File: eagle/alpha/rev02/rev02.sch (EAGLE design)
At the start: 404 parts, among them CN1 HOST, CN2 HOST, IC1 N25Q128A13ES, IC2 74AC244DW, IC3 N25Q128A13ES, IC4 74AC244DW, IC5 RCLAMP0502ASC-89, IC6 RCLAMP0502ASC-89, J1 STM32-SWD, Q1 2N7002, Q2 BC818, Q4 2N7002, Q5 ASFL1, Q6 2N7002, T1 BC847, T2 BC847, U1 LMZ13608, U10 ATTINY828R-AU, U12 23K640-I/SN, U13 XC7A200TFBG484, U14 EN6347QI, U15 EN6347QI, U16 EN5364QI, U2 LT3060ITS8-15, U3 MC74HC1G14DTT1G, U4 STM32F429BIT6, U5 IS45S32160F, U6 IS45S32160F, U7 MCP79412-I/SN, U8 FT232H_SERIAL, U9 FT232H_SERIAL, Y1 12 MHz, Y2 12 MHz

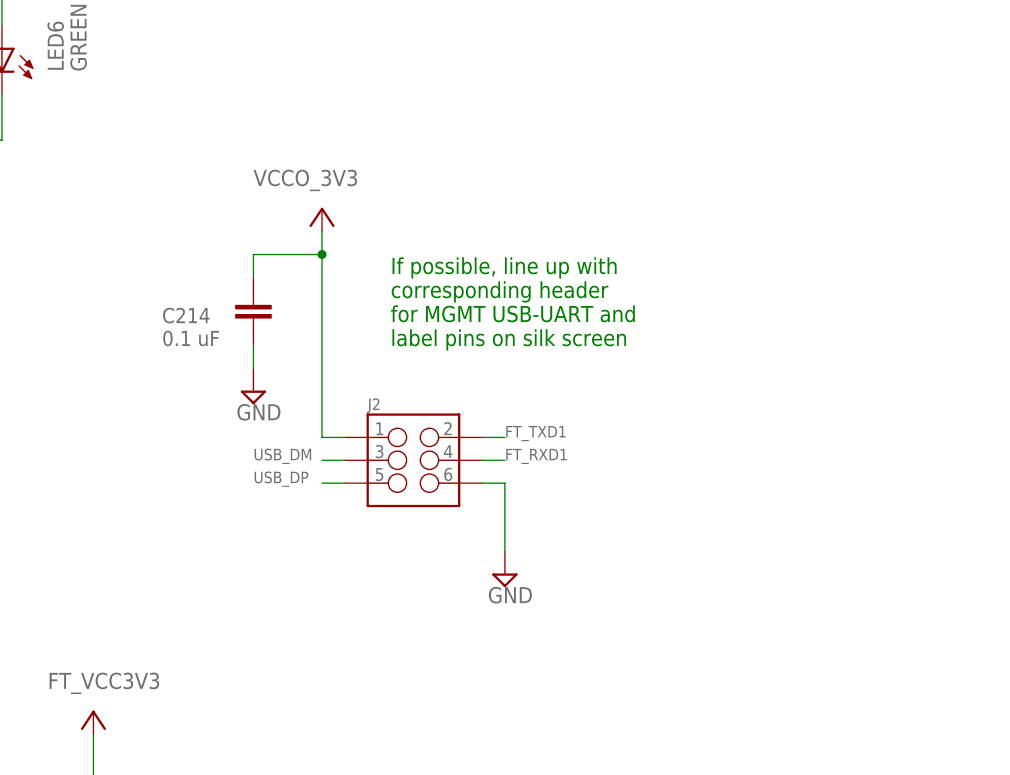
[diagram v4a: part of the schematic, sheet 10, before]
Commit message: Bugfix copy-paste mistake in USB MGMT UART header.
Also change pinout of header after input from Peter.
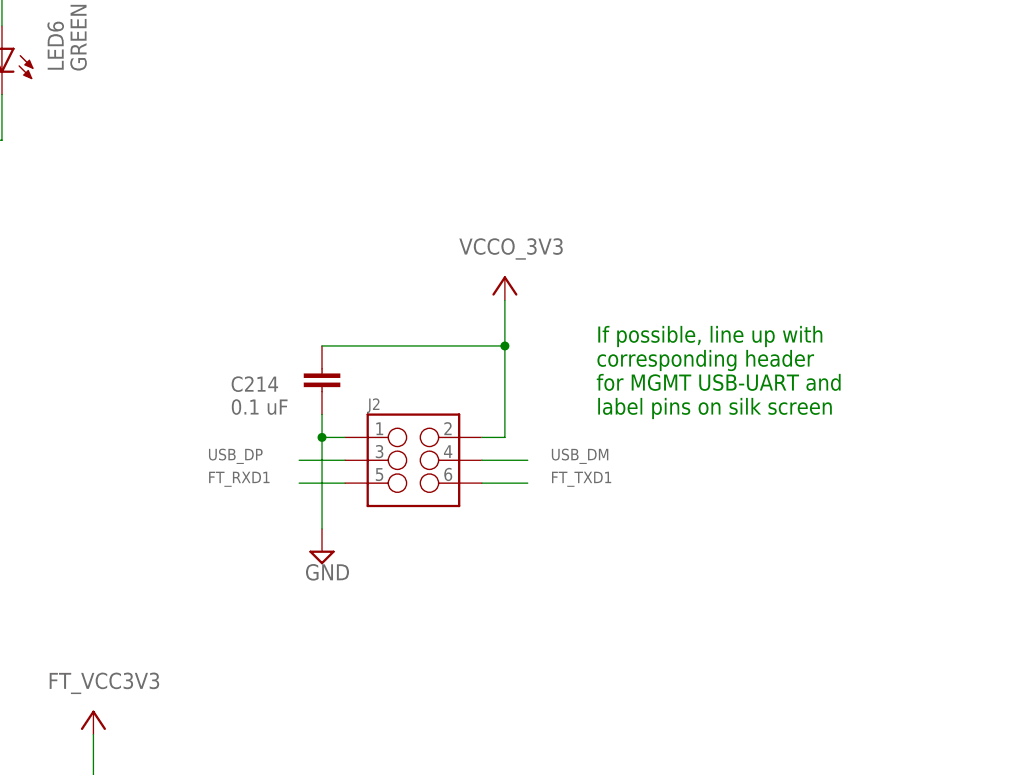
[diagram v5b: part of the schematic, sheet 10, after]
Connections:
- net FT_MGMT_RXD1: now also J3.5
- net FT_MGMT_TXD1: now also J3.6
- net FT_RXD1: now also J2.5; no longer J2.4, J3.4
- net FT_TXD1: now also J2.6; no longer J2.2, J3.2
- net GND: now also J2.1, J3.1; no longer J2.6, J3.6
- net USB_DM: no longer J2.3, J3.3
- net USB_DP: no longer J2.5, J3.5
- net USB_MGMT_DM: now also J3.4
- net USB_MGMT_DP: now also J3.3
- net VCCO_3V3: now also J2.2, J3.2; no longer J2.1, J3.1
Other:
- moved on the sheet: C214, C215
